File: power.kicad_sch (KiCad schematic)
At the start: 71 parts, among them SW1 SW_Push, U3 BD71847MWV, Y1 Crystal

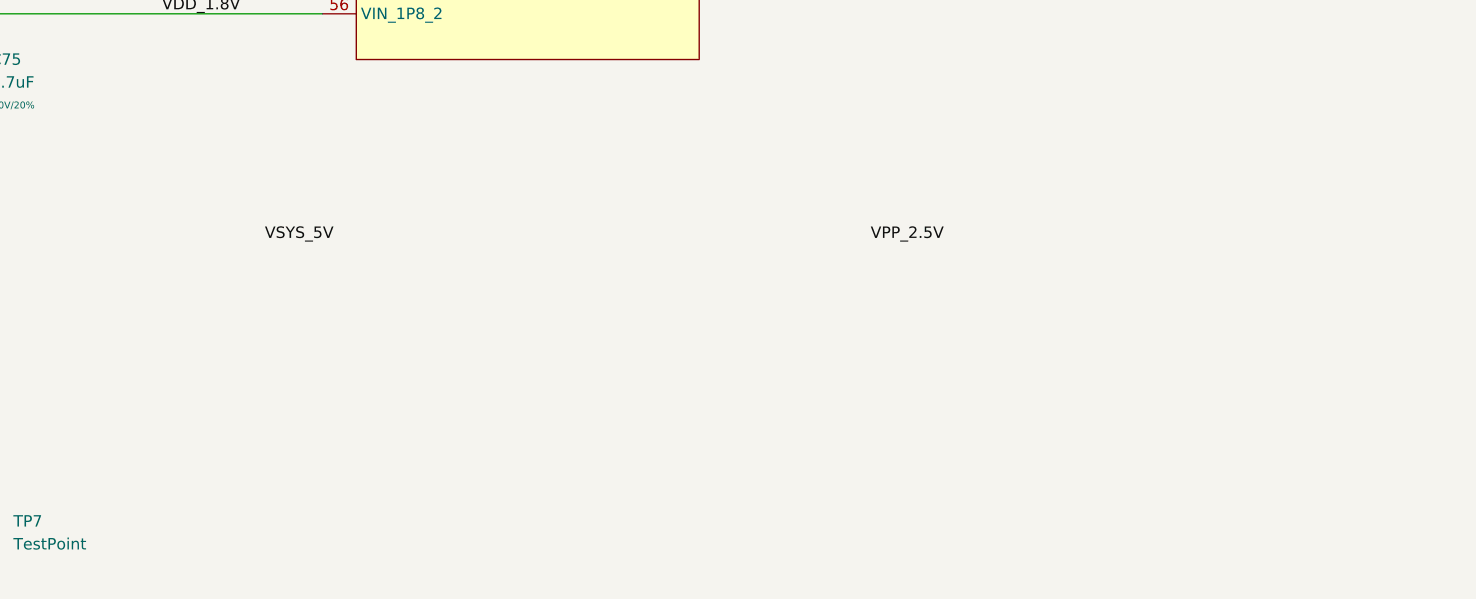
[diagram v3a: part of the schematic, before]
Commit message: add ddr vpp ldo, fix ddr net names
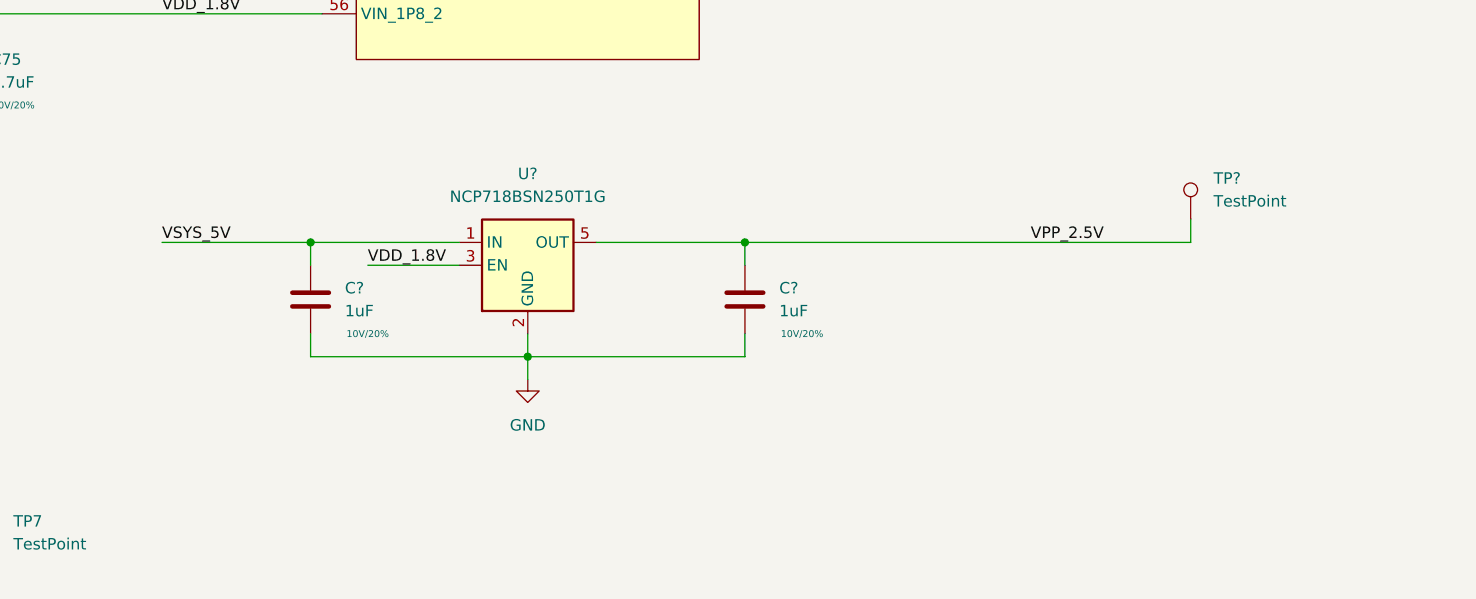
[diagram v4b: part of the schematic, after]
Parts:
- added C? (x2): 1uF, Capacitor_SMD:C_0402_1005Metric, symbol Device:C
- added TP?: TestPoint, TestPoint:TestPoint_Pad_D1.0mm, symbol Connector:TestPoint
- added U?: NCP718BSN250T1G, Package_TO_SOT_SMD:SOT-23-5, symbol Regulator_Linear:NCP718xSN250
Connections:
- net GND: now also C?.2, C?.2, U?.2 (GND)
- net VDD_1.8V: now also U?.3 (EN)
- net VPP_2.5V: now also C?.1, TP?.1, U?.5 (OUT)
- net VSYS_5V: now also C?.1, U?.1 (IN)
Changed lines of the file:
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@@
   (junction (at 115.57 120.65) (diameter 0) (color 0 0 0 0)
   )
+  (junction (at 123.19 345.44) (diameter 0) (color 0 0 0 0)
+  )
   (junction (at 358.14 195.58) (diameter 0) (color 0 0 0 0)
   )
@@
   (junction (at 95.25 80.01) (diameter 0) (color 0 0 0 0)
   )
+  (junction (at 147.32 358.14) (diameter 0) (color 0 0 0 0)
+  )
   (junction (at 172.72 67.31) (diameter 0) (color 0 0 0 0)
   )
   (junction (at 396.24 262.89) (diameter 0) (color 0 0 0 0)
   )
+  (junction (at 171.45 345.44) (diameter 0) (color 0 0 0 0)
+  )
   (junction (at 350.52 256.54) (diameter 0) (color 0 0 0 0)
   )
@@
     (stroke (width 0) (type default) (color 0 0 0 0))
   )
+  (wire (pts (xy 147.32 355.6) (xy 147.32 358.14))
+    (stroke (width 0) (type default) (color 0 0 0 0))
+  )
   (wire (pts (xy 115.57 80.01) (xy 121.92 80.01))
     (stroke (width 0) (type default) (color 0 0 0 0))
@@
     (stroke (width 0) (type default) (color 0 0 0 0))
   )
+  (wire (pts (xy 147.32 358.14) (xy 171.45 358.14))
+    (stroke (width 0) (type default) (color 0 0 0 0))
+  )
   (wire (pts (xy 95.25 64.77) (xy 95.25 80.01))
     (stroke (width 0) (type default) (color 0 0 0 0))
@@
     (stroke (width 0) (type default) (color 0 0 0 0))
   )
+  (wire (pts (xy 220.98 342.9) (xy 220.98 345.44))
+    (stroke (width 0) (type default) (color 0 0 0 0))
+  )
   (wire (pts (xy 35.56 58.42) (xy 59.69 58.42))
     (stroke (width 0) (type default) (color 0 0 0 0))
   )
+  (wire (pts (xy 106.68 345.44) (xy 123.19 345.44))
+    (stroke (width 0) (type default) (color 0 0 0 0))
+  )
   (wire (pts (xy 73.66 381) (xy 73.66 383.54))
     (stroke (width 0) (type default) (color 0 0 0 0))
@@
     (stroke (width 0) (type default) (color 0 0 0 0))
   )
+  (wire (pts (xy 123.19 358.14) (xy 147.32 358.14))
+    (stroke (width 0) (type default) (color 0 0 0 0))
+  )
   (wire (pts (xy 172.72 52.07) (xy 185.42 52.07))
     (stroke (width 0) (type default) (color 0 0 0 0))
@@
     (stroke (width 0) (type default) (color 0 0 0 0))
   )
+  (wire (pts (xy 123.19 345.44) (xy 139.7 345.44))
+    (stroke (width 0) (type default) (color 0 0 0 0))
+  )
   (wire (pts (xy 35.56 33.02) (xy 59.69 33.02))
     (stroke (width 0) (type default) (color 0 0 0 0))
@@
     (stroke (width 0) (type default) (color 0 0 0 0))
   )
+  (wire (pts (xy 154.94 345.44) (xy 171.45 345.44))
+    (stroke (width 0) (type default) (color 0 0 0 0))
+  )
   (wire (pts (xy 59.69 381) (xy 59.69 383.54))
     (stroke (width 0) (type default) (color 0 0 0 0))
@@
     (stroke (width 0) (type default) (color 0 0 0 0))
   )
+  (wire (pts (xy 171.45 345.44) (xy 220.98 345.44))
+    (stroke (width 0) (type default) (color 0 0 0 0))
+  )
+  (wire (pts (xy 171.45 345.44) (xy 171.45 347.98))
+    (stroke (width 0) (type default) (color 0 0 0 0))
+  )
   (wire (pts (xy 35.56 78.74) (xy 59.7644 78.74))
     (stroke (width 0) (type default) (color 0 0 0 0))
@@
     (stroke (width 0) (type default) (color 0 0 0 0))
   )
+  (wire (pts (xy 123.19 345.44) (xy 123.19 347.98))
+    (stroke (width 0) (type default) (color 0 0 0 0))
+  )
   (wire (pts (xy 115.57 80.01) (xy 115.57 82.55))
     (stroke (width 0) (type default) (color 0 0 0 0))
@@
     (stroke (width 0) (type default) (color 0 0 0 0))
   )
+  (wire (pts (xy 147.32 358.14) (xy 147.32 360.68))
+    (stroke (width 0) (type default) (color 0 0 0 0))
+  )
   (wire (pts (xy 35.56 40.64) (xy 59.69 40.64))
     (stroke (width 0) (type default) (color 0 0 0 0))
@@
     (stroke (width 0) (type default) (color 0 0 0 0))
   )
+  (wire (pts (xy 129.54 347.98) (xy 139.7 347.98))
+    (stroke (width 0) (type default) (color 0 0 0 0))
+  )
   (wire (pts (xy 327.66 165.1) (xy 337.82 165.1))
     (stroke (width 0) (type default) (color 0 0 0 0))
@@
     (stroke (width 0) (type default) (color 0 0 0 0))
   )
+  (wire (pts (xy 123.19 355.6) (xy 123.19 358.14))
+    (stroke (width 0) (type default) (color 0 0 0 0))
+  )
   (wire (pts (xy 264.16 123.19) (xy 264.16 125.73))
     (stroke (width 0) (type default) (color 0 0 0 0))
@@
     (stroke (width 0) (type default) (color 0 0 0 0))
   )
+  (wire (pts (xy 171.45 355.6) (xy 171.45 358.14))
+    (stroke (width 0) (type default) (color 0 0 0 0))
+  )
   (wire (pts (xy 269.24 105.41) (xy 269.24 107.95))
     (stroke (width 0) (type default) (color 0 0 0 0))
@@
     (effects (font (size 1.27 1.27)) (justify left bottom))
   )
-  (label "VSYS_5V" (at 118.11 345.44 0)
+  (label "VSYS_5V" (at 106.68 345.44 0)
     (effects (font (size 1.27 1.27)) (justify left bottom))
   )
@@
     (effects (font (size 1.27 1.27)) (justify left bottom))
   )
-  (label "VPP_2.5V" (at 185.42 345.44 0)
+  (label "VPP_2.5V" (at 203.2 345.44 0)
     (effects (font (size 1.27 1.27)) (justify left bottom))
   )
@@
     (effects (font (size 1.27 1.27)) (justify left bottom))
   )
+  (label "VDD_1.8V" (at 129.54 347.98 0)
+    (effects (font (size 1.27 1.27)) (justify left bottom))
+  )
   (label "PMIC_ON_REQ" (at 38.1 63.5 0)
     (effects (font (size 1.27 1.27)) (justify left bottom))
@@
     (pin "1")
   )
+  (symbol (lib_id "power:GND") (at 147.32 360.68 0) (unit 1)
+    (in_bom yes) (on_board yes) (fields_autoplaced)
+    (property "Reference" "#PWR?" (id 0) (at 147.32 367.03 0)
+      (effects (font (size 1.27 1.27)) hide)
+    )
+    (property "Value" "GND" (id 1) (at 147.32 365.76 0))
+    (property "Footprint" "" (id 2) (at 147.32 360.68 0)
+      (effects (font (size 1.27 1.27)) hide)
+    )
+    (property "Datasheet" "" (id 3) (at 147.32 360.68 0)
+      (effects (font (size 1.27 1.27)) hide)
+    )
+    (pin "1")
+  )
   (symbol (lib_id "power:GND") (at 115.57 151.13 0) (unit 1)
     (in_bom yes) (on_board yes) (fields_autoplaced)
@@
     (pin "1")
   )
+  (symbol (lib_id "Connector:TestPoint") (at 220.98 342.9 0) (unit 1)
+    (in_bom yes) (on_board yes) (fields_autoplaced)
+    (property "Reference" "TP?" (id 0) (at 223.52 338.3279 0)
+      (effects (font (size 1.27 1.27)) (justify left))
+    )
+    (property "Value" "TestPoint" (id 1) (at 223.52 340.8679 0)
+      (effects (font (size 1.27 1.27)) (justify left))
+    )
+    (property "Footprint" "TestPoint:TestPoint_Pad_D1.0mm" (id 2) (at 226.06 342.9 0)
+      (effects (font (size 1.27 1.27)) hide)
+    )
+    (property "Datasheet" "~" (id 3) (at 226.06 342.9 0)
+      (effects (font (size 1.27 1.27)) hide)
+    )
+    (pin "1")
+  )
   (symbol (lib_id "Device:C") (at 317.5 73.66 0) (unit 1)
     (in_bom yes) (on_board yes)
@@
     (pin "2")
   )
+  (symbol (lib_id "Regulator_Linear:NCP718xSN250") (at 147.32 347.98 0) (unit 1)
+    (in_bom yes) (on_board yes) (fields_autoplaced)
+    (property "Reference" "U?" (id 0) (at 147.32 337.82 0))
+    (property "Value" "NCP718BSN250T1G" (id 1) (at 147.32 340.36 0))
+    (property "Footprint" "Package_TO_SOT_SMD:SOT-23-5" (id 2) (at 147.32 339.09 0)
+      (effects (font (size 1.27 1.27)) hide)
+    )
+    (property "Datasheet" "https://www.onsemi.com/pub/Collateral/NCP718-D.PDF" (id 3) (at 147.32 335.28 0)
+      (effects (font (size 1.27 1.27)) hide)
+    )
+    (pin "1")
+    (pin "2")
+    (pin "3")
+    (pin "4")
+    (pin "5")
+  )
   (symbol (lib_id "Device:C") (at 193.04 198.12 0) (unit 1)
     (in_bom yes) (on_board yes)
@@
     (pin "2")
   )
+  (symbol (lib_id "Device:C") (at 123.19 351.79 0) (unit 1)
+    (in_bom yes) (on_board yes)
+    (property "Reference" "C?" (id 0) (at 127 350.5199 0)
+      (effects (font (size 1.27 1.27)) (justify left))
+    )
+    (property "Value" "1uF" (id 1) (at 127 353.0599 0)
+      (effects (font (size 1.27 1.27)) (justify left))
+    )
+    (property "Footprint" "Capacitor_SMD:C_0402_1005Metric" (id 2) (at 124.1552 355.6 0)
+      (effects (font (size 1.27 1.27)) hide)
+    )
+    (property "Datasheet" "~" (id 3) (at 123.19 351.79 0)
+      (effects (font (size 1.27 1.27)) hide)
+    )
+    (property "Rating" "10V/20%" (id 4) (at 129.54 355.6 0)
+      (effects (font (size 0.762 0.762)))
+    )
+    (pin "1")
+    (pin "2")
+  )
   (symbol (lib_id "Device:L") (at 189.23 123.19 90) (unit 1)
     (in_bom yes) (on_board yes) (fields_autoplaced)
@@
       (effects (font (size 0.762 0.762)))
     )
+    (pin "1")
+    (pin "2")
+  )
+  (symbol (lib_id "Device:C") (at 171.45 351.79 0) (unit 1)
+    (in_bom yes) (on_board yes)
+    (property "Reference" "C?" (id 0) (at 175.26 350.5199 0)
+      (effects (font (size 1.27 1.27)) (justify left))
+    )
+    (property "Value" "1uF" (id 1) (at 175.26 353.0599 0)
+      (effects (font (size 1.27 1.27)) (justify left))
+    )
+    (property "Footprint" "Capacitor_SMD:C_0402_1005Metric" (id 2) (at 172.4152 355.6 0)
+      (effects (font (size 1.27 1.27)) hide)
+    )
+    (property "Datasheet" "~" (id 3) (at 171.45 351.79 0)
+      (effects (font (size 1.27 1.27)) hide)
+    )
+    (property "Rating" "10V/20%" (id 4) (at 177.8 355.6 0)
+      (effects (font (size 0.762 0.762)))
+    )

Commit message: add inital ddr tool version, lots of routing work
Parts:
- gave numbers to parts that had none: 4
- renumbered C98 to C100, C99 to C101, C100 to C102, C101 to C103, C102 to C104, C103 to C105, C104 to C106, C105 to C107, C106 to C108, C84 to C86, C85 to C87, C86 to C88, C87 to C89, C88 to C90, C89 to C91, C90 to C92, C91 to C93, C92 to C94, C93 to C95, C94 to C96, C95 to C97, C96 to C98, C97 to C99, TP18 to TP19, TP19 to TP20, TP20 to TP21, TP21 to TP22, TP22 to TP23
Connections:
- net NVCC_DRAM_1.2V: no longer C93.1, C94.1, L6.2, TP10.1
- net NVCC_SNVS_1P8 renamed NVCC_SNVS_1.8
- new net VDD_DRAM_1.2V: C93.1, C94.1, L6.2, TP10.1
